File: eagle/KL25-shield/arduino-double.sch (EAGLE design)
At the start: 19 parts, among them U1 ARDUINO_SHIELDNO_SILK

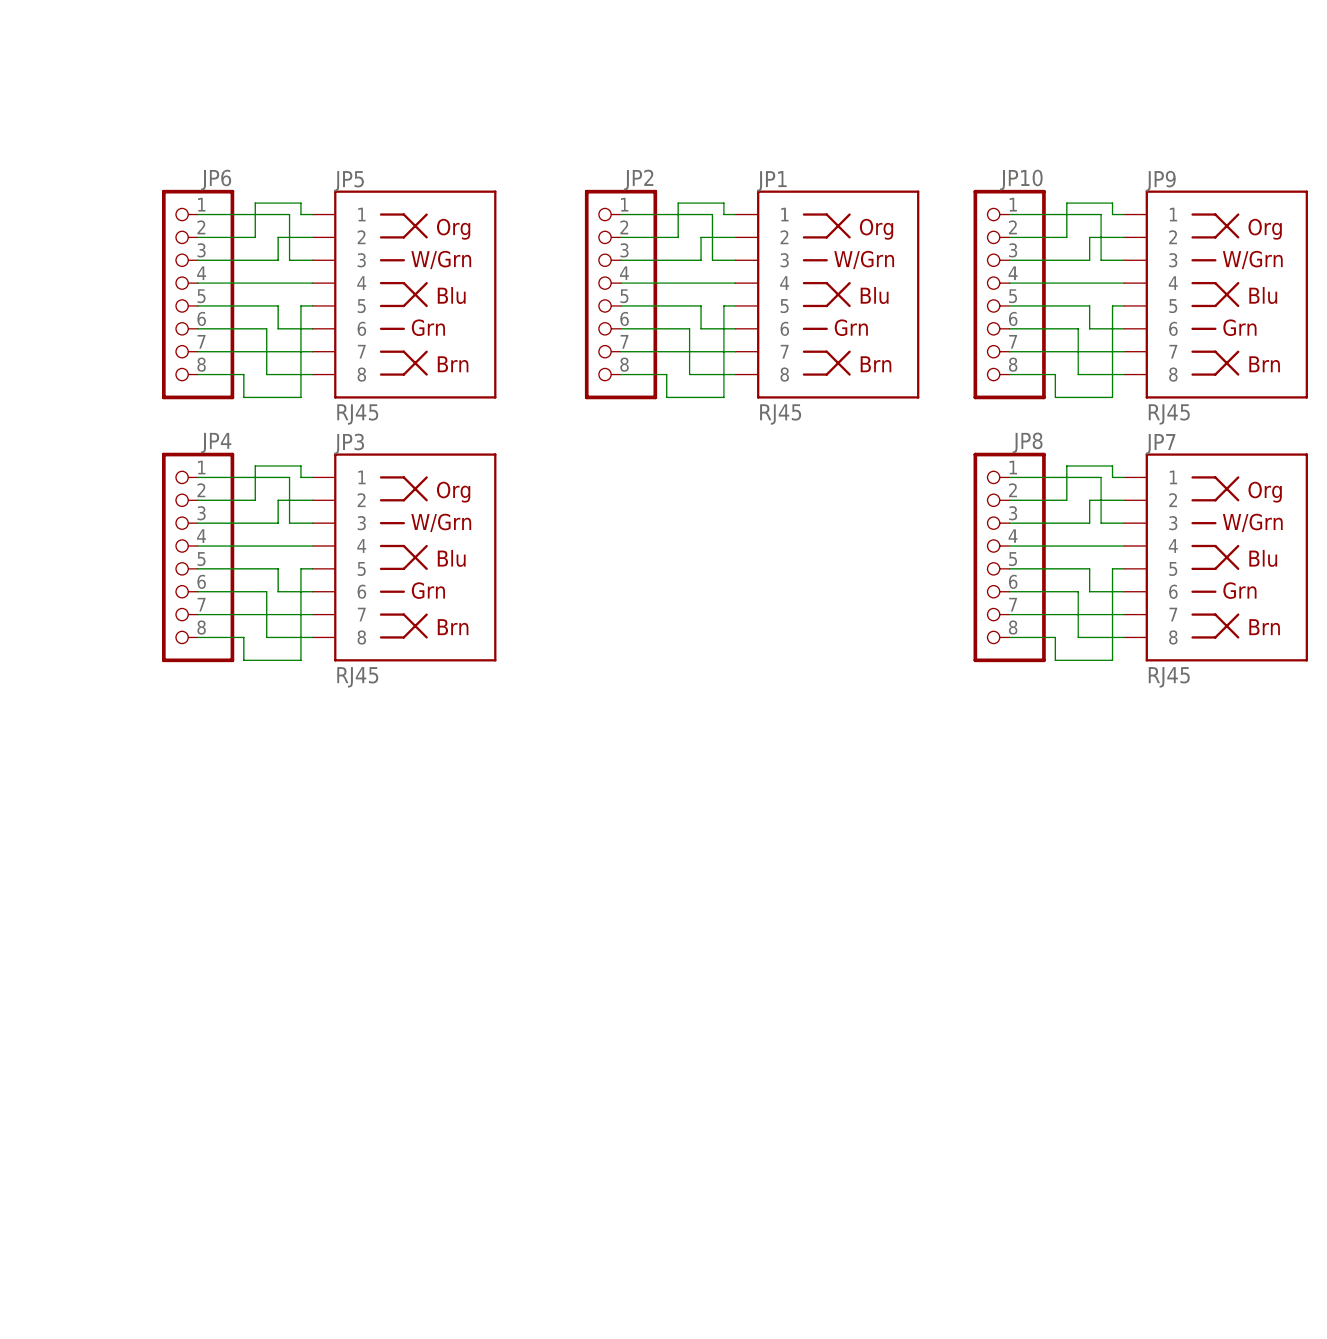
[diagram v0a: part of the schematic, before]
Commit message: RJ45 - 8x1 pinhead mapping to make routing with no crossings
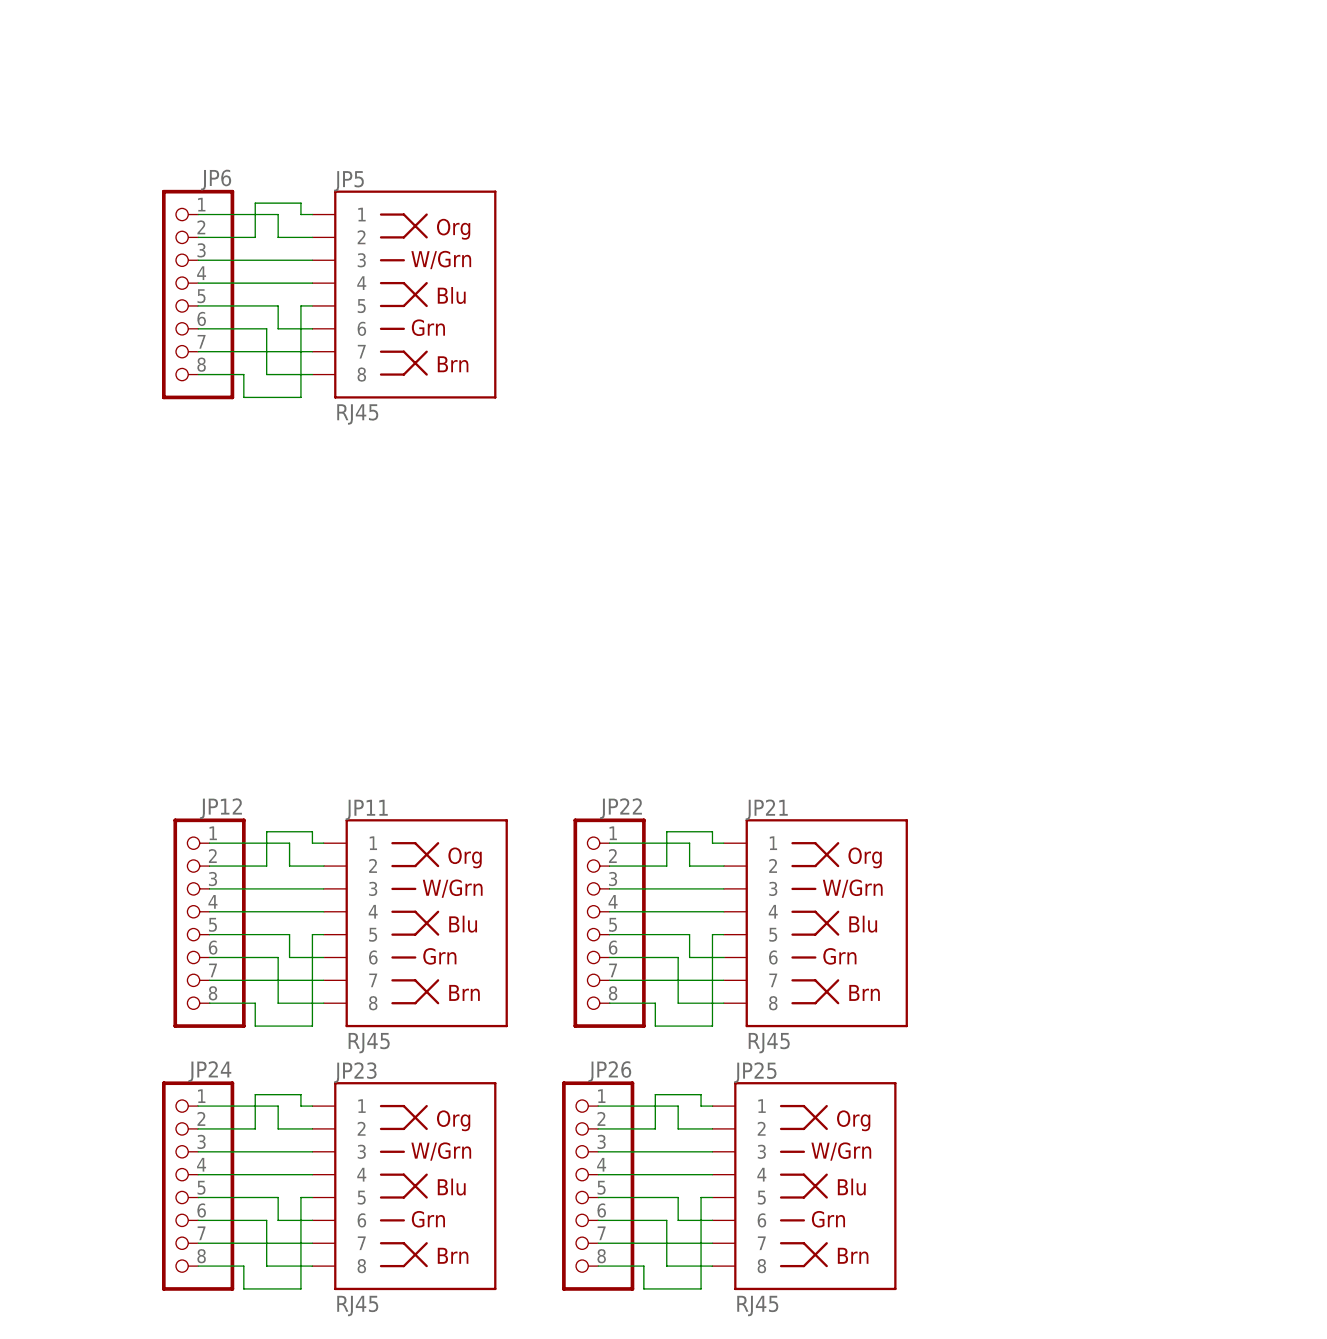
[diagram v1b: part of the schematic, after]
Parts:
- removed JP1, JP3, JP7, JP9: RJ45, dbg-misc:RJ45-8PTH
- removed JP10, JP2, JP4, JP8: (no value), pinhead:PINHD-1X8
- added JP11, JP21, JP23, JP25: RJ45, dbg-misc:RJ45-8PTH
- added JP12, JP22, JP24, JP26: (no value), pinhead:PINHD-1X8
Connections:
- removed net N$57: JP1.2, JP2.3
- removed net N$58: JP1.4, JP2.4
- removed net N$59: JP1.6, JP2.5
- removed net N$60: JP1.8, JP2.6
- removed net N$61: JP1.1, JP2.2
- removed net N$62: JP1.5, JP2.8
- removed net N$63: JP1.7, JP2.7
- removed net N$64: JP1.3, JP2.1
- removed net N$65: JP3.2, JP4.3
- removed net N$66: JP3.4, JP4.4
- removed net N$67: JP3.6, JP4.5
- removed net N$68: JP3.8, JP4.6
- removed net N$69: JP3.1, JP4.2
- removed net N$70: JP3.5, JP4.8
- removed net N$71: JP3.7, JP4.7
- removed net N$72: JP3.3, JP4.1
- removed net N$81: JP7.2, JP8.3
- removed net N$82: JP7.4, JP8.4
- removed net N$83: JP7.6, JP8.5
- removed net N$84: JP7.8, JP8.6
- removed net N$85: JP7.1, JP8.2
- removed net N$86: JP7.5, JP8.8
- removed net N$87: JP7.7, JP8.7
- removed net N$88: JP7.3, JP8.1
- removed net N$89: JP10.3, JP9.2
- removed net N$90: JP10.4, JP9.4
- removed net N$91: JP10.5, JP9.6
- removed net N$92: JP10.6, JP9.8
- removed net N$93: JP10.2, JP9.1
- removed net N$94: JP10.8, JP9.5
- removed net N$95: JP10.7, JP9.7
- removed net N$96: JP10.1, JP9.3
- new net N$100: JP11.8, JP12.6
- new net N$101: JP11.1, JP12.2
- new net N$102: JP11.5, JP12.8
- new net N$103: JP11.7, JP12.7
- new net N$104: JP11.2, JP12.1
- new net N$106: JP21.3, JP22.3
- new net N$107: JP21.4, JP22.4
- new net N$108: JP21.6, JP22.5
- new net N$109: JP21.8, JP22.6
- new net N$110: JP21.1, JP22.2
- new net N$111: JP21.5, JP22.8
- new net N$112: JP21.7, JP22.7
- new net N$113: JP21.2, JP22.1
- new net N$114: JP23.3, JP24.3
- new net N$115: JP23.4, JP24.4
- new net N$116: JP23.6, JP24.5
- new net N$117: JP23.8, JP24.6
- new net N$118: JP23.1, JP24.2
- new net N$119: JP23.5, JP24.8
- new net N$120: JP23.7, JP24.7
- new net N$121: JP23.2, JP24.1
- new net N$122: JP25.3, JP26.3
- new net N$123: JP25.4, JP26.4
- new net N$124: JP25.6, JP26.5
- new net N$125: JP25.8, JP26.6
- new net N$126: JP25.1, JP26.2
- new net N$127: JP25.5, JP26.8
- new net N$128: JP25.7, JP26.7
- new net N$129: JP25.2, JP26.1
- new net N$97: JP11.3, JP12.3
- new net N$98: JP11.4, JP12.4
- new net N$99: JP11.6, JP12.5
- net N$73: now also JP5.3; no longer JP5.2
- net N$80: now also JP5.2; no longer JP5.3

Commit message: KL25 shield, board and pdf
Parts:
- added JP1, JP2, JP3, JP4: (no value), pinhead:PINHD-1X2
- added JP10, JP27, JP28, JP29, JP30, JP31, JP32, JP33, JP34, JP35, JP36, JP37, JP38, JP7, JP8, JP9: (no value), pinhead:PINHD-1X6
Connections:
- new net N$57: JP1.1, U1.B12
- new net N$58: JP1.2, U1.B13
- new net N$59: JP2.1, U1.B14
- new net N$60: JP2.2, U1.B15
- new net N$61: JP3.1, U1.D16
- new net N$62: JP3.2, U1.D17
- new net N$63: JP4.1, U1.D18
- new net N$64: JP4.2, U1.D19
- new net N$65: JP7.1, JP7.2, JP7.3, JP7.4, JP7.5, JP7.6
- new net N$70: JP8.1, JP8.2, JP8.3, JP8.4, JP8.5, JP8.6
- new net N$71: JP9.1, JP9.2, JP9.3, JP9.4, JP9.5, JP9.6
- new net N$72: JP10.1, JP10.2, JP10.3, JP10.4, JP10.5, JP10.6
- new net N$81: JP27.1, JP27.2, JP27.3, JP27.4, JP27.5, JP27.6
- new net N$82: JP28.1, JP28.2, JP28.3, JP28.4, JP28.5, JP28.6
- new net N$83: JP29.1, JP29.2, JP29.3, JP29.4, JP29.5, JP29.6
- new net N$84: JP30.1, JP30.2, JP30.3, JP30.4, JP30.5, JP30.6
- new net N$85: JP31.1, JP31.2, JP31.3, JP31.4, JP31.5, JP31.6
- new net N$86: JP32.1, JP32.2, JP32.3, JP32.4, JP32.5, JP32.6
- new net N$87: JP33.1, JP33.2, JP33.3, JP33.4, JP33.5, JP33.6
- new net N$88: JP34.1, JP34.2, JP34.3, JP34.4, JP34.5, JP34.6
- new net N$89: JP35.1, JP35.2, JP35.3, JP35.4, JP35.5, JP35.6
- new net N$90: JP36.1, JP36.2, JP36.3, JP36.4, JP36.5, JP36.6
- new net N$91: JP37.1, JP37.2, JP37.3, JP37.4, JP37.5, JP37.6
- new net N$92: JP38.1, JP38.2, JP38.3, JP38.4, JP38.5, JP38.6
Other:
- moved on the sheet: JP19, JP20
